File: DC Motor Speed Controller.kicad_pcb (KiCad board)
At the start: 2 copper layers, 64.8 x 30.8 mm, 15 parts, among them J1 Screw_Terminal_01x02, J2 Screw_Terminal_01x02, Q1 TIP122, U1 NE555P

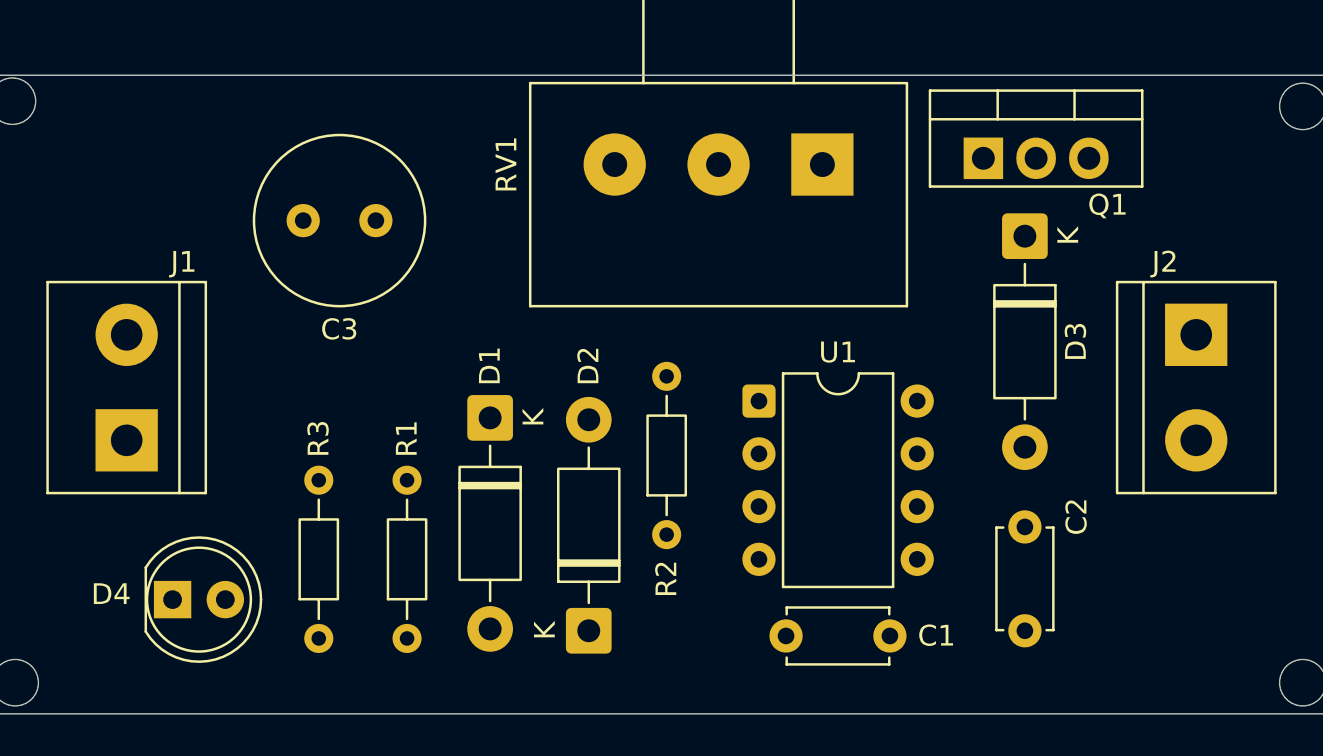
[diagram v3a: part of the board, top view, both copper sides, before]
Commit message: Added Tracks to PCB
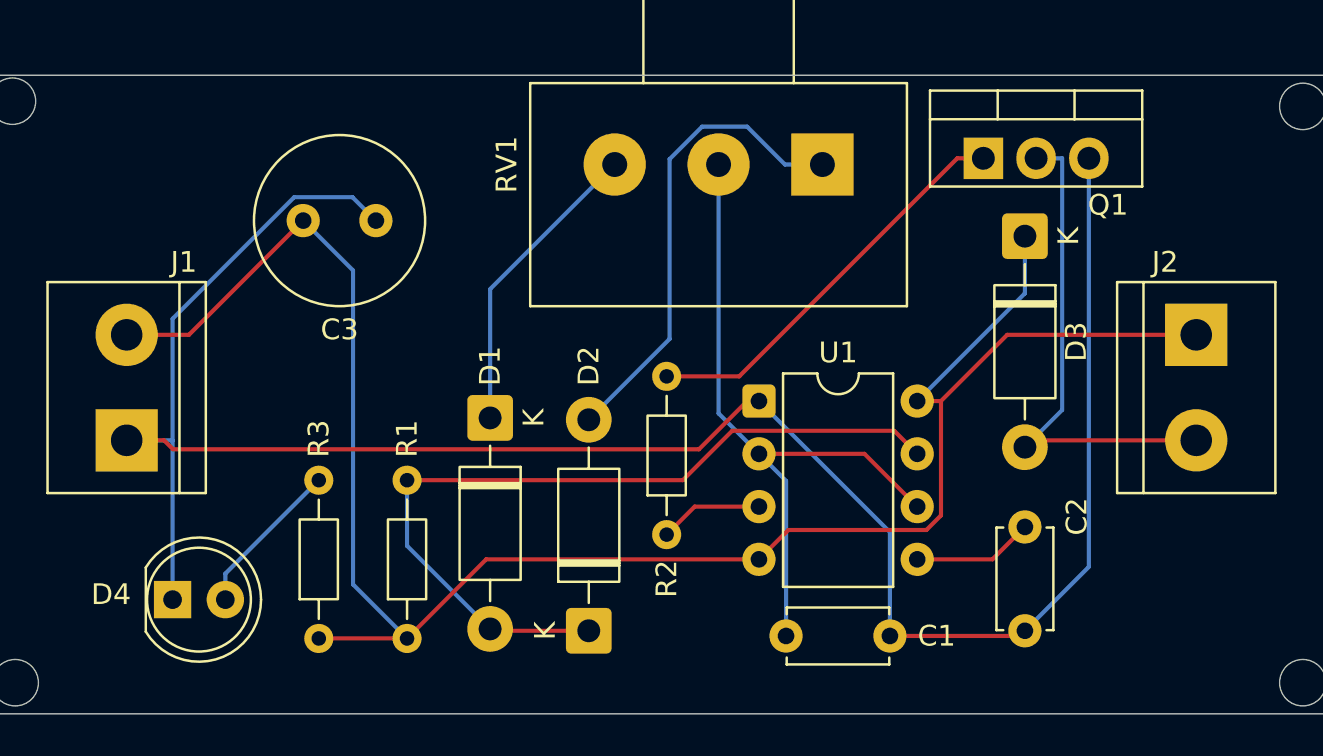
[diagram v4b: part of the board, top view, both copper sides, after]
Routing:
- net GND: track 0.00 -> 104.5 mm
- net Net-(D3-K): track 0.00 -> 95.7 mm
- net Net-(D1-A): track 0.00 -> 39.6 mm
- net Net-(U1-THR): track 0.00 -> 32.7 mm
- net Net-(D3-A): track 0.00 -> 24.3 mm
- net Net-(D2-A): track 0.00 -> 22.9 mm
- net Net-(Q1-B): track 0.00 -> 19.6 mm
- net Net-(D1-K): track 0.00 -> 14.7 mm
- net Net-(D4-A): track 0.00 -> 7.61 mm
- net Net-(U1-CV): track 0.00 -> 5.83 mm
- net Net-(U1-Q): track 0.00 -> 5.00 mm

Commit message: Added Round Tracks to PCB
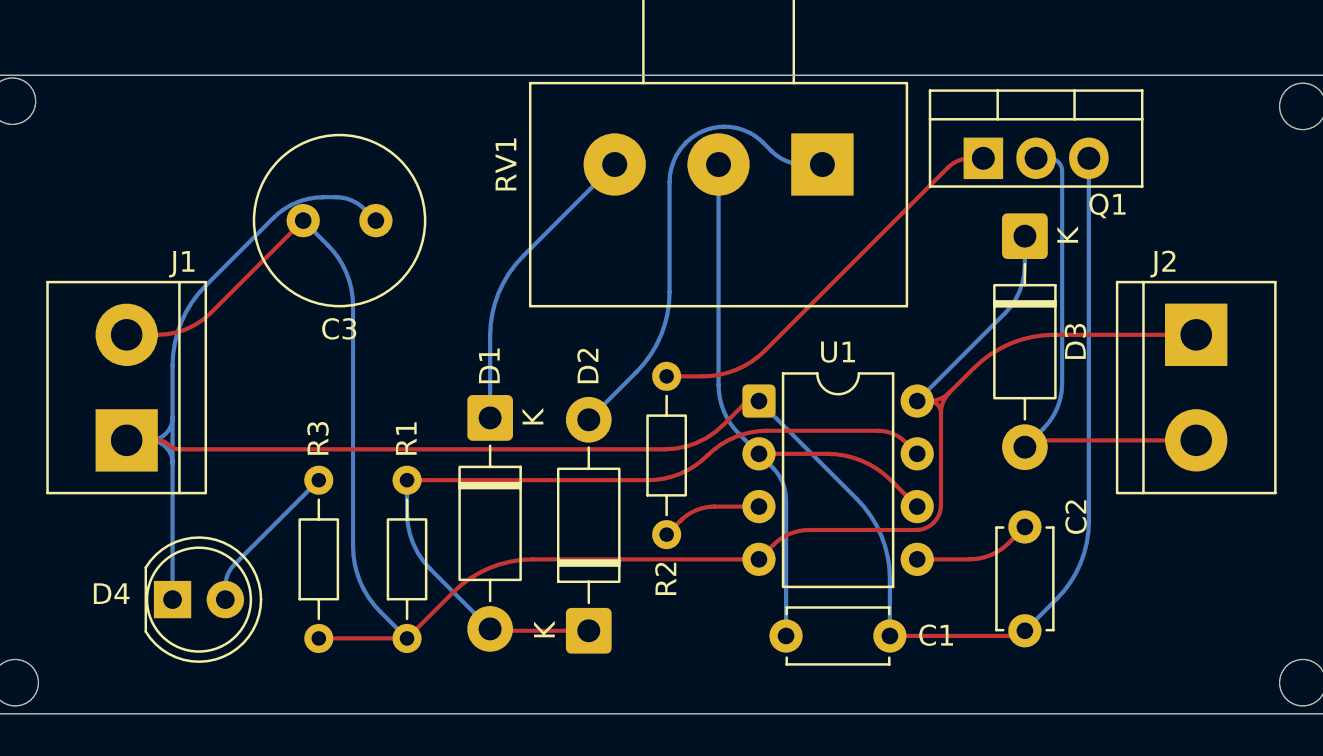
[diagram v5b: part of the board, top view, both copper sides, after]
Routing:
- net GND: track 104.5 -> 105.5 mm
- net Net-(D2-A): track 22.9 -> 22.2 mm
- net Net-(D1-A): track 39.6 -> 38.9 mm
